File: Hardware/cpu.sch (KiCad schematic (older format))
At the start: 18 parts, among them U13 STM32F411CEU6, Y2 Crystal_Small, Y3 Crystal_GND24

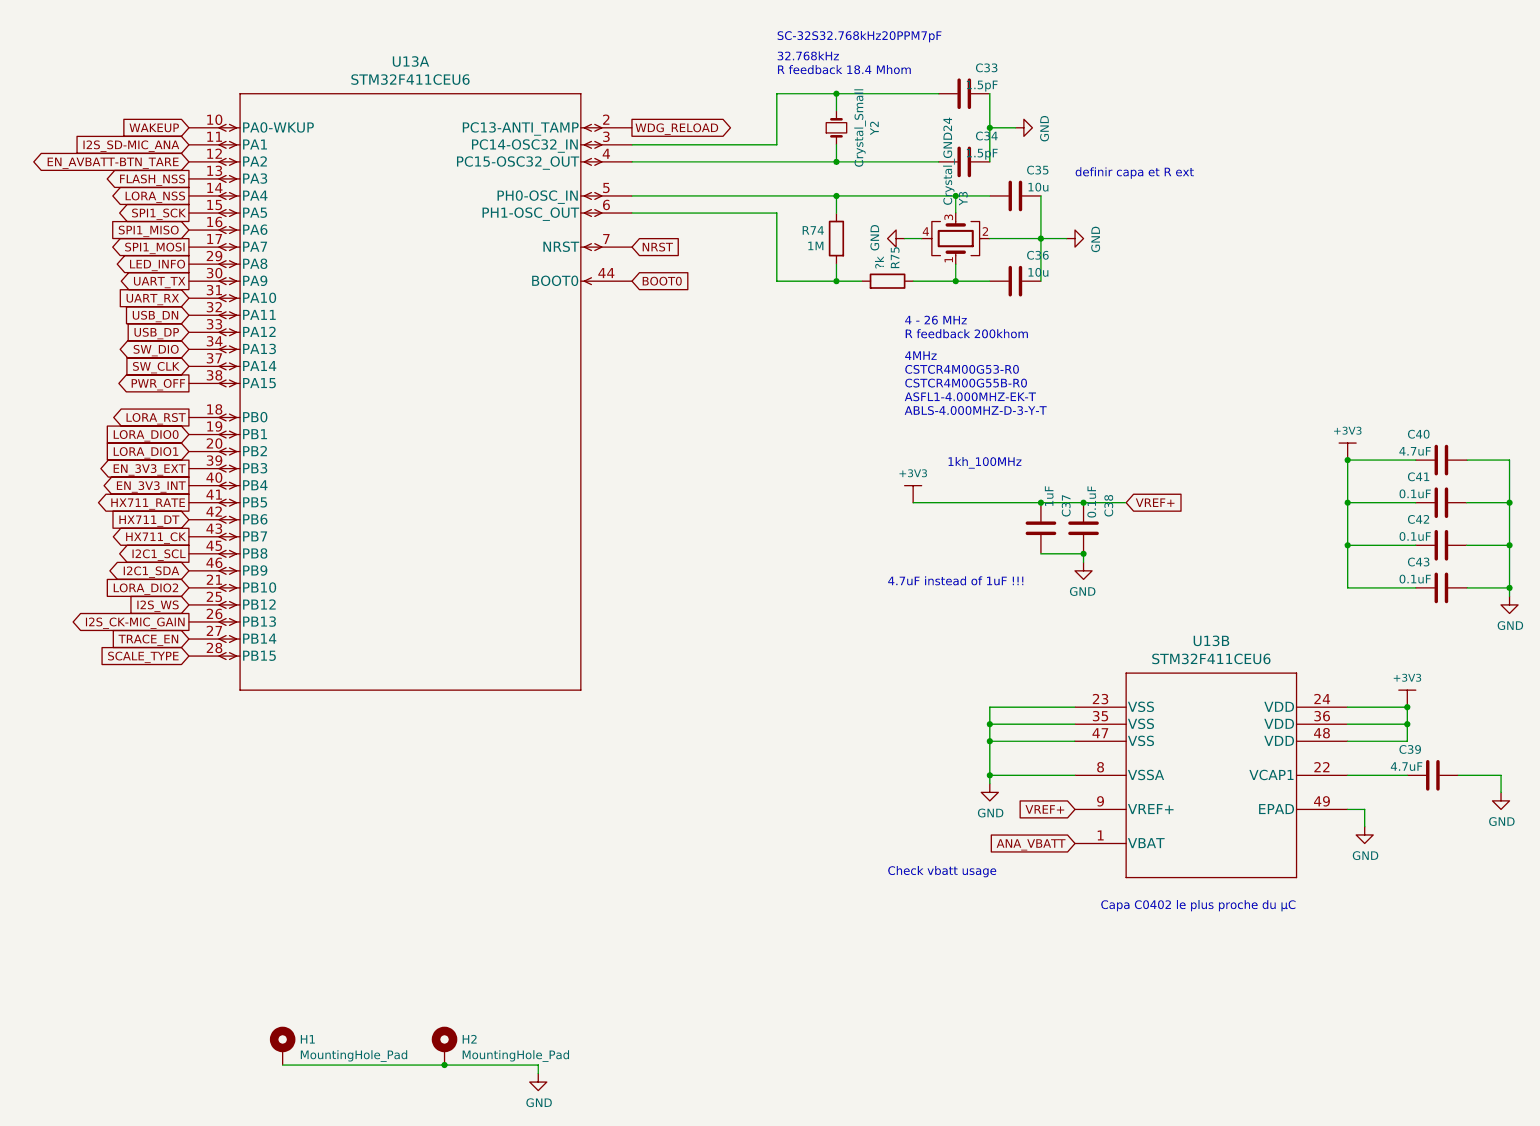
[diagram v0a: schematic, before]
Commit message: Add pcb route and ground plane
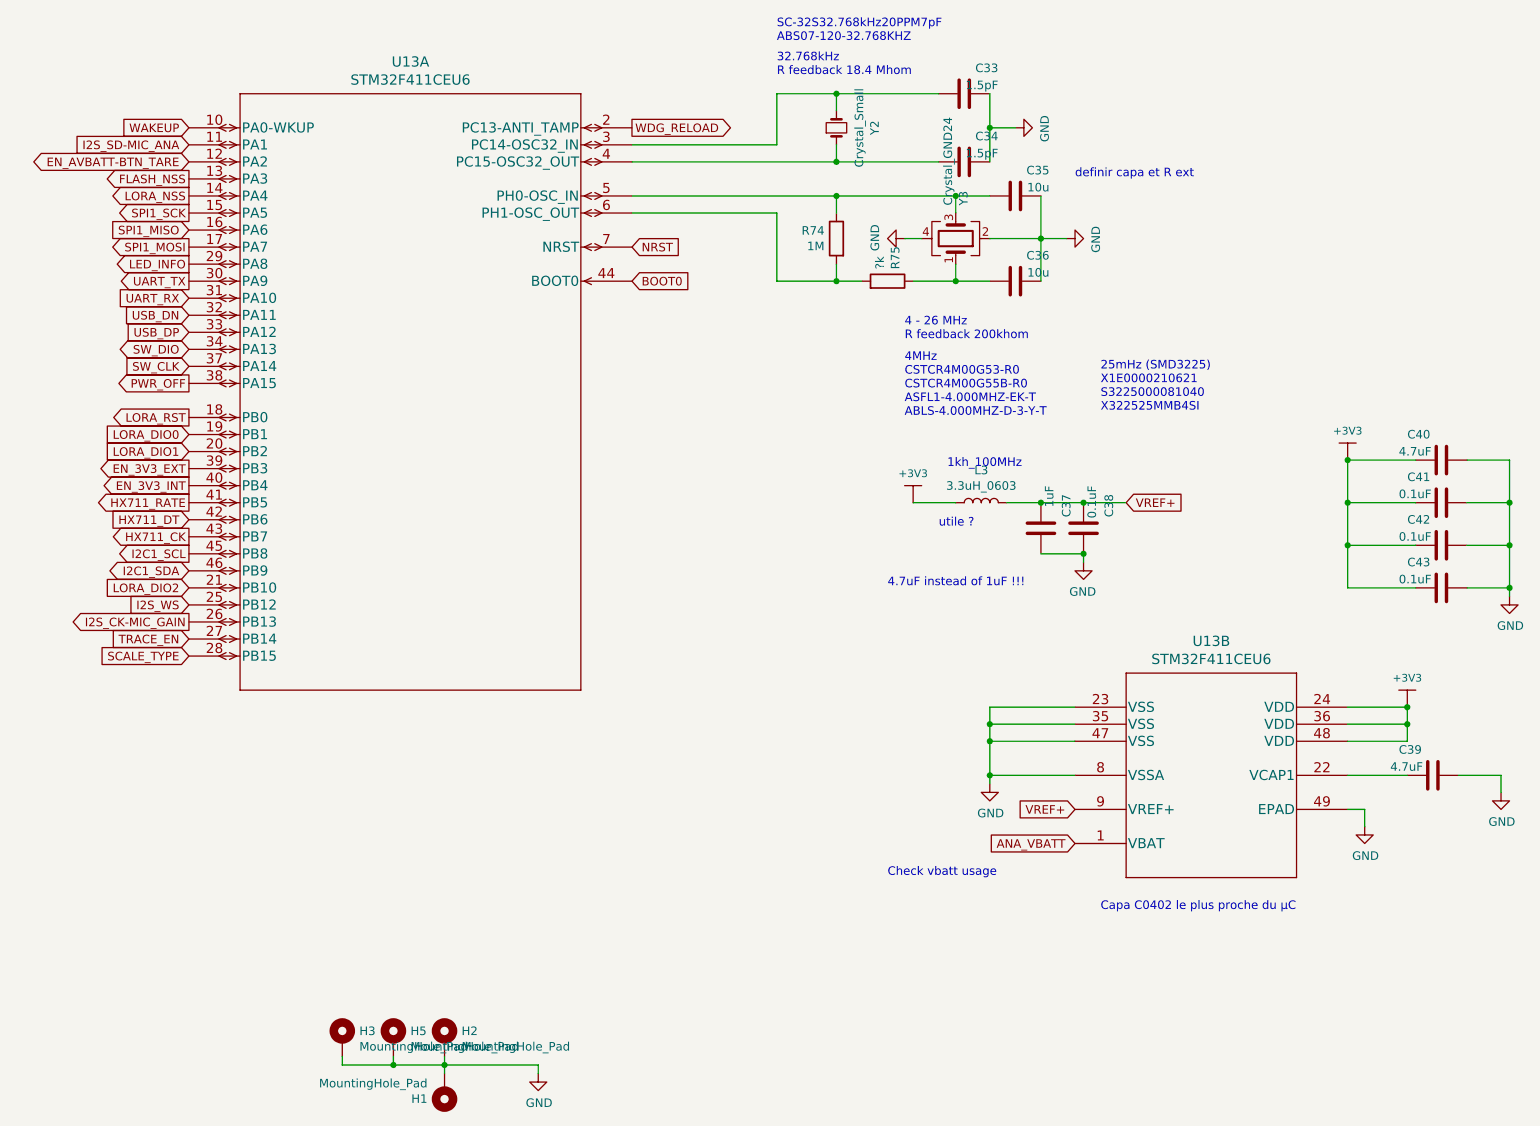
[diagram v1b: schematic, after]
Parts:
- added H3, H5: MountingHole_Pad, MountingHole:MountingHole_2.7mm_M2.5_Pad_Via, symbol Mechanical:MountingHole_Pad
- added L3: 3.3uH_0603, Inductor_SMD:L_0402_1005Metric, symbol Device:L
- C33, C34, C35, C36, C37, C38, C39, C40, C41, C42, C43: footprint Capacitor_SMD:C_0603_1608Metric -> Capacitor_SMD:C_0201_0603Metric
- H1, H2: footprint MountingHole:MountingHole_2.7mm -> MountingHole:MountingHole_2.7mm_M2.5_Pad_Via
- R74, R75: footprint Resistor_SMD:R_0603_1608Metric -> Resistor_SMD:R_0201_0603Metric
- U13: footprint (none) -> EcoApi_pcb:STM32F411CEU6
- Y2: footprint (none) -> EcoApi_pcb:XTAL_ABS07-120-32.768KHZ-T
- Y3: footprint (none) -> EcoApi_pcb:X322525MMB4SI
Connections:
- net +3V3: now also L3.1; no longer C37.2, C38.2, U13.9 (VREF+)
- net GND: now also H3.1, H5.1
- new net VREF+: C37.2, C38.2, L3.2, U13.9 (VREF+)
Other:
- note added: "25mHz (SMD3225)\nX1E0000210621\nS3225000081040\nX322525MMB4SI\n\n"
- note added: "SC-32S32.768kHz20PPM7pF\nABS07-120-32.768KHZ"
- note added: "utile ?"
- note removed: "SC-32S32.768kHz20PPM7pF\n"
- moved on the sheet: H1, H2
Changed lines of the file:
@@
 L Mechanical:MountingHole_Pad H?
 U 1 1 62BA86F0
-P 4050 6750
+P 4050 6700
 AR Path="/62BA86F0" Ref="H?"  Part="1"
 AR Path="/62B8145A/62BA86F0" Ref="H2"  Part="1"
-F 0 "H2" H 4150 6799 50  0000 L CNN
-F 1 "MountingHole_Pad" H 4150 6708 50  0000 L CNN
-F 2 "MountingHole:MountingHole_2.7mm" H 4050 6750 50  0001 C CNN
-F 3 "~" H 4050 6750 50  0001 C CNN
-	1    4050 6750
+F 0 "H2" H 4150 6749 50  0000 L CNN
+F 1 "MountingHole_Pad" H 4150 6658 50  0000 L CNN
+F 2 "MountingHole:MountingHole_2.7mm_M2.5_Pad_Via" H 4050 6700 50  0001 C CNN
+F 3 "~" H 4050 6700 50  0001 C CNN
+	1    4050 6700
 	1    0    0    -1
 $EndComp
@@
 L Mechanical:MountingHole_Pad H?
 U 1 1 62BA86F6
-P 3100 6750
+P 4050 7000
 AR Path="/62BA86F6" Ref="H?"  Part="1"
 AR Path="/62B8145A/62BA86F6" Ref="H1"  Part="1"
-F 0 "H1" H 3200 6799 50  0000 L CNN
-F 1 "MountingHole_Pad" H 3200 6708 50  0000 L CNN
-F 2 "MountingHole:MountingHole_2.7mm" H 3100 6750 50  0001 C CNN
-F 3 "~" H 3100 6750 50  0001 C CNN
-	1    3100 6750
-	1    0    0    -1
+F 0 "H1" H 4150 7049 50  0000 L CNN
+F 1 "MountingHole_Pad" H 4150 6958 50  0000 L CNN
+F 2 "MountingHole:MountingHole_2.7mm_M2.5_Pad_Via" H 4050 7000 50  0001 C CNN
+F 3 "~" H 4050 7000 50  0001 C CNN
+	1    4050 7000
+	-1   0    0    1
 $EndComp
 $Comp
@@
 $EndComp
 Wire Wire Line
-	3100 6850 4050 6850
-Wire Wire Line
 	4600 6850 4600 6900
-Connection ~ 4050 6850
-Wire Wire Line
-	4050 6850 4600 6850
 Text Notes 6650 5750 0    50   ~ 0
 Check vbatt usage\n
@@
 F 0 "C39" V 10000 4950 50  0000 L CNN
 F 1 "4.7uF" V 9900 4900 50  0000 L CNN
-F 2 "Capacitor_SMD:C_0603_1608Metric" H 9888 5000 50  0001 C CNN
+F 2 "Capacitor_SMD:C_0201_0603Metric" H 9888 5000 50  0001 C CNN
 F 3 "~" H 9850 5150 50  0001 C CNN
 	1    9850 5150
@@
 F 0 "U13" H 8550 5137 60  0000 C CNN
 F 1 "STM32F411CEU6" H 8550 5031 60  0000 C CNN
-F 2 "" H 8550 4990 60  0001 C CNN
+F 2 "EcoApi_pcb:STM32F411CEU6" H 8550 4990 60  0001 C CNN
 F 3 "" H 7750 4750 60  0000 C CNN
 	2    7750 4750
@@
 F 0 "C41" V 10050 3350 50  0000 L CNN
 F 1 "0.1uF" V 9950 3300 50  0000 L CNN
-F 2 "Capacitor_SMD:C_0603_1608Metric" H 9938 3400 50  0001 C CNN
+F 2 "Capacitor_SMD:C_0201_0603Metric" H 9938 3400 50  0001 C CNN
 F 3 "~" H 9900 3550 50  0001 C CNN
 	1    9900 3550
@@
 F 0 "C42" V 10050 3600 50  0000 L CNN
 F 1 "0.1uF" V 9950 3550 50  0000 L CNN
-F 2 "Capacitor_SMD:C_0603_1608Metric" H 9938 3650 50  0001 C CNN
+F 2 "Capacitor_SMD:C_0201_0603Metric" H 9938 3650 50  0001 C CNN
 F 3 "~" H 9900 3800 50  0001 C CNN
 	1    9900 3800
@@
 F 0 "C43" V 10050 3850 50  0000 L CNN
 F 1 "0.1uF" V 9950 3800 50  0000 L CNN
-F 2 "Capacitor_SMD:C_0603_1608Metric" H 9938 3900 50  0001 C CNN
+F 2 "Capacitor_SMD:C_0201_0603Metric" H 9938 3900 50  0001 C CNN
 F 3 "~" H 9900 4050 50  0001 C CNN
 	1    9900 4050
@@
 F 0 "C37" V 7700 3500 50  0000 L CNN
 F 1 "1uF" V 7600 3450 50  0000 L CNN
-F 2 "Capacitor_SMD:C_0603_1608Metric" H 7588 3550 50  0001 C CNN
+F 2 "Capacitor_SMD:C_0201_0603Metric" H 7588 3550 50  0001 C CNN
 F 3 "~" H 7550 3700 50  0001 C CNN
 	1    7550 3700
@@
 F 0 "C38" V 7950 3500 50  0000 L CNN
 F 1 "0.1uF" V 7850 3450 50  0000 L CNN
-F 2 "Capacitor_SMD:C_0603_1608Metric" H 7838 3550 50  0001 C CNN
+F 2 "Capacitor_SMD:C_0201_0603Metric" H 7838 3550 50  0001 C CNN
 F 3 "~" H 7800 3700 50  0001 C CNN
 	1    7800 3700
@@
 F 0 "C40" V 10050 3100 50  0000 L CNN
 F 1 "4.7uF" V 9950 3050 50  0000 L CNN
-F 2 "Capacitor_SMD:C_0603_1608Metric" H 9938 3150 50  0001 C CNN
+F 2 "Capacitor_SMD:C_0201_0603Metric" H 9938 3150 50  0001 C CNN
 F 3 "~" H 9900 3300 50  0001 C CNN
 	1    9900 3300
@@
 Wire Wire Line
 	7800 3550 7550 3550
-Connection ~ 7550 3550
 Text Notes 7900 5950 0    50   ~ 0
 Capa C0402 le plus proche du µC
@@
 F 0 "Y3" H 7244 2046 50  0000 L CNN
 F 1 "Crystal_GND24" H 7244 1955 50  0000 L CNN
-F 2 "" H 7050 2000 50  0001 C CNN
+F 2 "EcoApi_pcb:X322525MMB4SI" H 7050 2000 50  0001 C CNN
 F 3 "~" H 7050 2000 50  0001 C CNN
 	1    7050 2000
@@
 F 0 "C35" V 7550 1550 50  0000 L CNN
 F 1 "10u" V 7450 1550 50  0000 L CNN
-F 2 "Capacitor_SMD:C_0603_1608Metric" H 7438 1600 50  0001 C CNN
+F 2 "Capacitor_SMD:C_0201_0603Metric" H 7438 1600 50  0001 C CNN
 F 3 "~" H 7400 1750 50  0001 C CNN
 	1    7400 1750
@@
 F 0 "C36" V 7550 2050 50  0000 L CNN
 F 1 "10u" V 7450 2050 50  0000 L CNN
-F 2 "Capacitor_SMD:C_0603_1608Metric" H 7438 2100 50  0001 C CNN
+F 2 "Capacitor_SMD:C_0201_0603Metric" H 7438 2100 50  0001 C CNN
 F 3 "~" H 7400 2250 50  0001 C CNN
 	1    7400 2250
@@
 F 0 "R75" H 6720 2296 50  0000 L CNN
 F 1 "?k" H 6720 2205 50  0000 L CNN
-F 2 "Resistor_SMD:R_0603_1608Metric" V 6580 2250 50  0001 C CNN
+F 2 "Resistor_SMD:R_0201_0603Metric" V 6580 2250 50  0001 C CNN
 F 3 "~" H 6650 2250 50  0001 C CNN
 	1    6650 2250
@@
 F 0 "R74" H 6420 2046 50  0000 L CNN
 F 1 "1M" H 6420 1955 50  0000 L CNN
-F 2 "Resistor_SMD:R_0603_1608Metric" V 6280 2000 50  0001 C CNN
+F 2 "Resistor_SMD:R_0201_0603Metric" V 6280 2000 50  0001 C CNN
 F 3 "~" H 6350 2000 50  0001 C CNN
 	1    6350 2000
@@
 F 0 "Y2" H 6350 1575 50  0000 C CNN
 F 1 "Crystal_Small" H 6350 1484 50  0000 C CNN
-F 2 "" H 6350 1350 50  0001 C CNN
+F 2 "EcoApi_pcb:XTAL_ABS07-120-32.768KHZ-T" H 6350 1350 50  0001 C CNN
 F 3 "~" H 6350 1350 50  0001 C CNN
 	1    6350 1350
@@
 F 0 "U13" H 3850 1737 60  0000 C CNN
 F 1 "STM32F411CEU6" H 3850 1631 60  0000 C CNN
-F 2 "" H 3350 1590 60  0001 C CNN
+F 2 "EcoApi_pcb:STM32F411CEU6" H 3350 1590 60  0001 C CNN
 F 3 "" H 2550 1350 60  0000 C CNN
 	1    2550 1350
@@
 4MHz\nCSTCR4M00G53-R0\nCSTCR4M00G55B-R0\nASFL1-4.000MHZ-EK-T\nABLS-4.000MHZ-D-3-Y-T
 Text Notes 6000 850  0    50   ~ 0
-SC-32S32.768kHz20PPM7pF\n
+SC-32S32.768kHz20PPM7pF\nABS07-120-32.768KHZ
 Text Notes 7750 1650 0    50   ~ 0
 definir capa et R ext
@@
 F 0 "C34" V 7250 1350 50  0000 L CNN
 F 1 "1.5pF" V 7150 1350 50  0000 L CNN
-F 2 "Capacitor_SMD:C_0603_1608Metric" H 7138 1400 50  0001 C CNN
+F 2 "Capacitor_SMD:C_0201_0603Metric" H 7138 1400 50  0001 C CNN
 F 3 "~" H 7100 1550 50  0001 C CNN
 	1    7100 1550
@@
 F 0 "C33" V 7250 950 50  0000 L CNN
 F 1 "1.5pF" V 7150 950 50  0000 L CNN
-F 2 "Capacitor_SMD:C_0603_1608Metric" H 7138 1000 50  0001 C CNN
+F 2 "Capacitor_SMD:C_0201_0603Metric" H 7138 1000 50  0001 C CNN
 F 3 "~" H 7100 1150 50  0001 C CNN
 	1    7100 1150
@@
 Text Notes 7000 3350 0    50   ~ 0
 1kh_100MHz
-Wire Wire Line
-	6800 3550 7550 3550
+Text Notes 7900 3100 0    50   ~ 0
+25mHz (SMD3225)\nX1E0000210621\nS3225000081040\nX322525MMB4SI\n\n
+$Comp
+L Mechanical:MountingHole_Pad H?
+U 1 1 63B128D4
+P 3450 6700
+AR Path="/63B128D4" Ref="H?"  Part="1"
+AR Path="/62B8145A/63B128D4" Ref="H3"  Part="1"
+F 0 "H3" H 3550 6749 50  0000 L CNN
+F 1 "MountingHole_Pad" H 3550 6658 50  0000 L CNN
+F 2 "MountingHole:MountingHole_2.7mm_M2.5_Pad_Via" H 3450 6700 50  0001 C CNN
+F 3 "~" H 3450 6700 50  0001 C CNN
+	1    3450 6700
+	1    0    0    -1
+$EndComp
+$Comp
+L Mechanical:MountingHole_Pad H?
+U 1 1 63B14935
+P 3750 6700
+AR Path="/63B14935" Ref="H?"  Part="1"
+AR Path="/62B8145A/63B14935" Ref="H5"  Part="1"
+F 0 "H5" H 3850 6749 50  0000 L CNN
+F 1 "MountingHole_Pad" H 3850 6658 50  0000 L CNN
+F 2 "MountingHole:MountingHole_2.7mm_M2.5_Pad_Via" H 3750 6700 50  0001 C CNN
+F 3 "~" H 3750 6700 50  0001 C CNN
+	1    3750 6700
+	1    0    0    -1
+$EndComp
+Wire Wire Line
+	3450 6850 3750 6850
+Wire Wire Line
+	4050 6800 4050 6850
+Connection ~ 4050 6850
+Wire Wire Line
+	4050 6850 4600 6850
+Wire Wire Line
+	4050 6850 4050 6900
+Wire Wire Line
+	3750 6800 3750 6850
+Connection ~ 3750 6850
+Wire Wire Line
+	3750 6850 4050 6850
+Wire Wire Line
+	3450 6800 3450 6850
+$Comp
+L Device:L L?
+U 1 1 63D4FB09
+P 7200 3550
+AR Path="/62CC297B/63D4FB09" Ref="L?"  Part="1"
+AR Path="/62EA3721/63D4FB09" Ref="L?"  Part="1"
+AR Path="/62B8145A/63D4FB09" Ref="L3"  Part="1"
+F 0 "L3" V 7390 3550 50  0000 C CNN
+F 1 "3.3uH_0603" V 7299 3550 50  0000 C CNN
+F 2 "Inductor_SMD:L_0402_1005Metric" H 7200 3550 50  0001 C CNN
+F 3 "~" H 7200 3550 50  0001 C CNN
+	1    7200 3550
+	0    -1   -1   0
+$EndComp
+Wire Wire Line
+	7050 3550 6800 3550
+Text Notes 6950 3700 0    50   ~ 0
+utile ?
+Wire Wire Line
+	7350 3550 7550 3550
+Connection ~ 7550 3550
 $EndSCHEMATC
